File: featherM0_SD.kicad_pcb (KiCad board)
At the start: 2 copper layers, 50.8 x 22.9 mm, 34 parts, among them J1 10118194-0001LF, J2 503182-1853, SW1 SPST_TACT-KMR2, U1 ATSAMD21G18A-AUT, U2 SPX3819-3.3, U3 MCP73831T-2ACI/OT, X1 JSTPH, X2 32.768

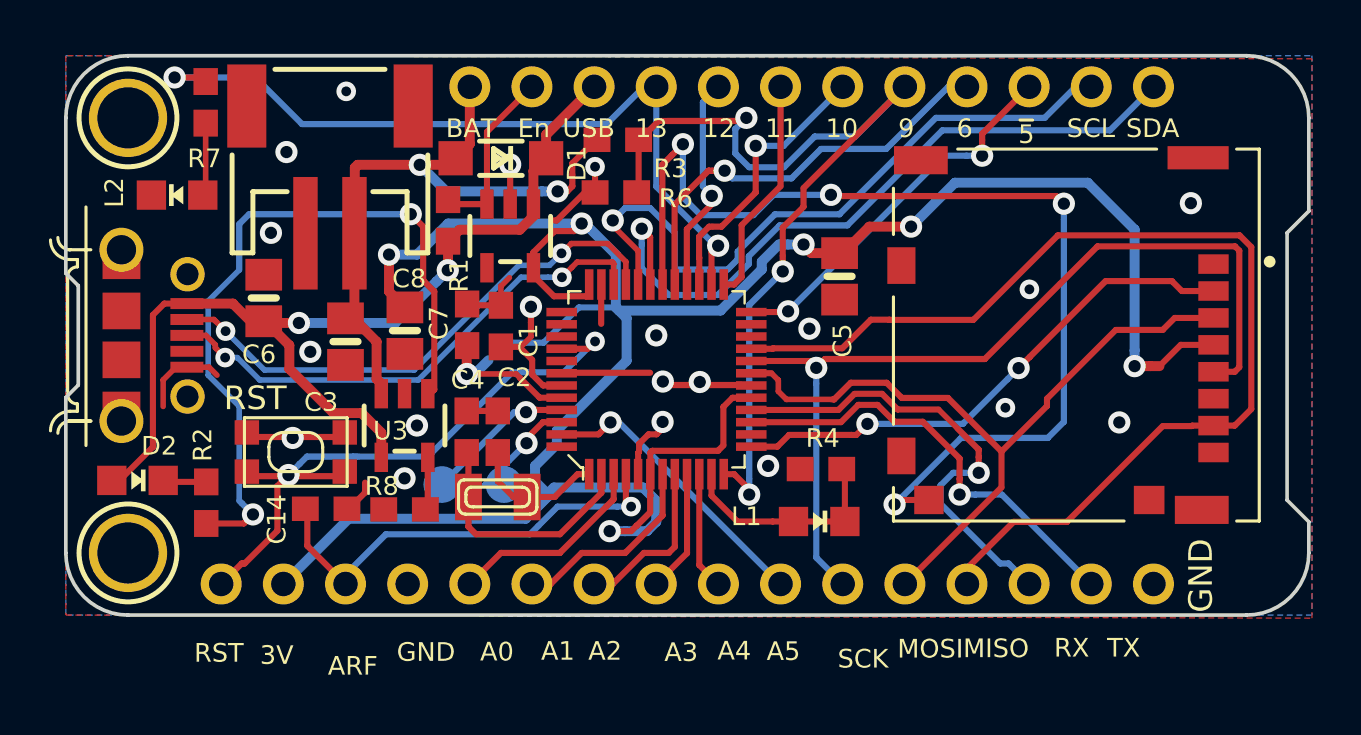
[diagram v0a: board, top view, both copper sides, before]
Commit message: cleaned up silkscreen
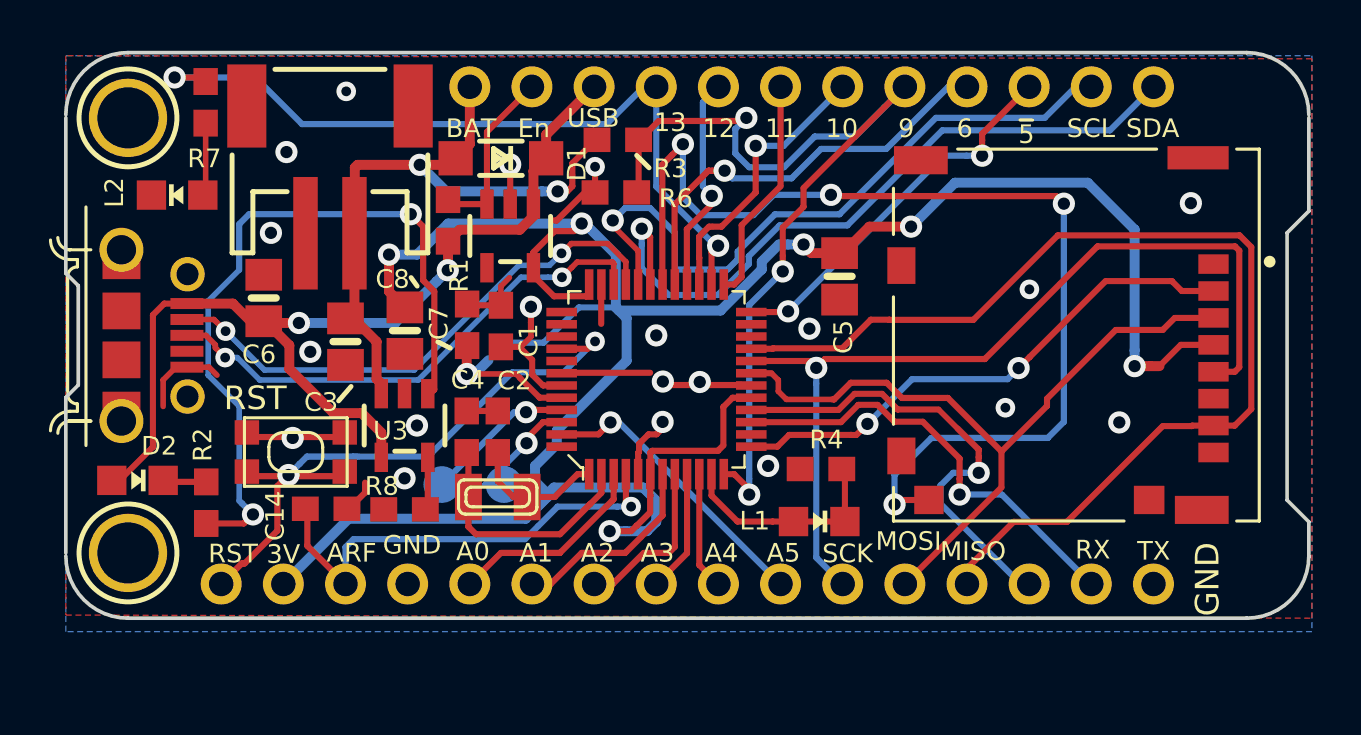
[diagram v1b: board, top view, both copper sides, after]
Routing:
- net /D7: track 43.7 -> 44.4 mm
- net /AREF: track 18.8 -> 19.5 mm
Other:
- board size 50.8 x 22.9 mm -> 50.8 x 23.1 mm
- net class Default: clearance 0.1778 -> 0.1524; trace_width 0.2286 -> 0.1524; via_dia 0.8 -> 0.6858; via_drill 0.4 -> 0.3302
- rule pad_to_mask_clearance: 0.2 -> 0.0508
- rule trace_clearance: 0.1778 -> 0.1524
- rule trace_min: 0.1016 -> 0.1524
- rule via_min_drill: 0.3 -> 0.254
- rule via_min_size: 0.4 -> 0.508

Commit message: cleaned up board outline
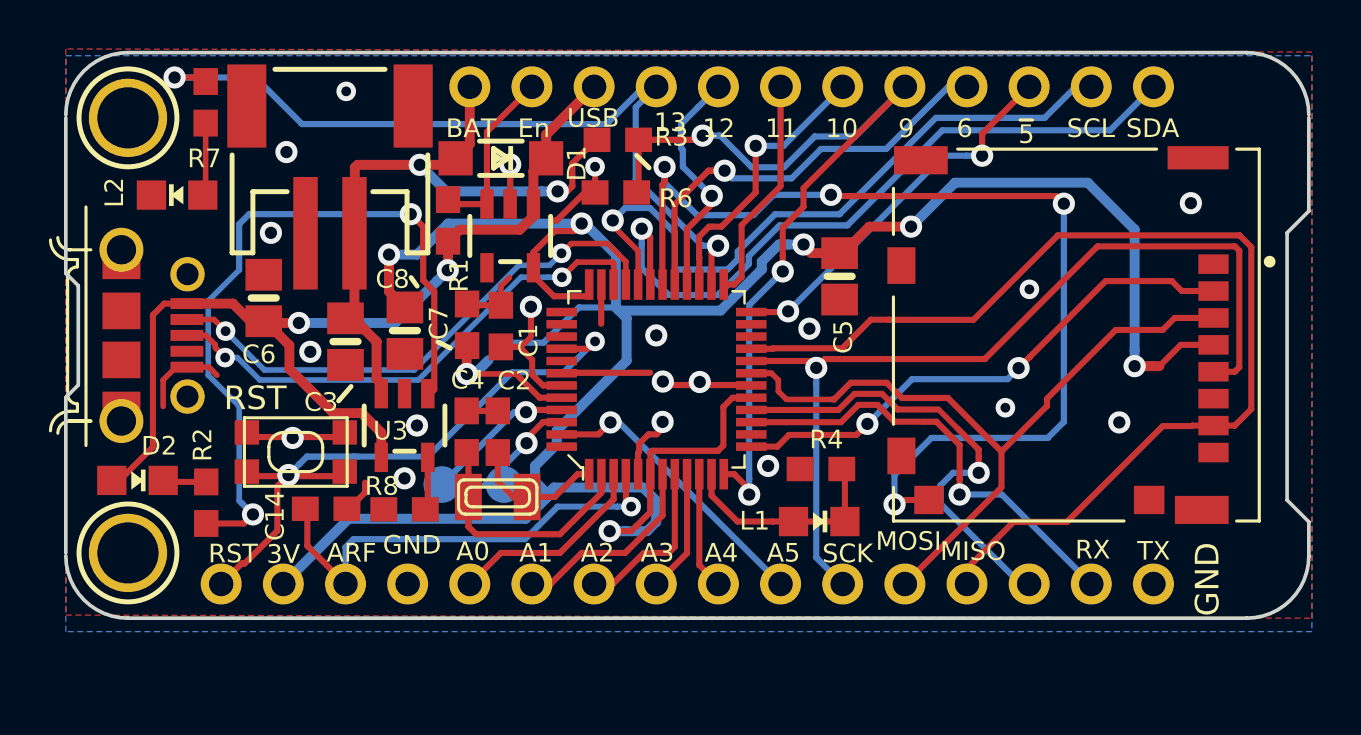
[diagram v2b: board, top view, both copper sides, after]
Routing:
- net /D9: track 38.1 -> 36.1 mm
- net /D7: track 44.4 -> 42.7 mm
- net /D13: track 31.8 -> 32.8 mm
- net /D12: track 9.40 -> 10.1 mm
